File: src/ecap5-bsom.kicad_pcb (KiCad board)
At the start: 6 copper layers, 69.6 x 30 mm, 178 parts, among them J13 DDR4_SODIMM_Board, U1 TPS565242DRDR, U10 IS42S16160J-*BL, U11 IS43DR86400E, U12 ASFC4G31M-51*, U2 TPS562202DRLR, U3 TPS562202DRLR, U4 TPS562202DRLR, U5 LM3880MF*-1AA, U6 LFE5U-85F-*BG756*, U7 XLH335040.000000I, U8 W25Q128JVPIQ, U9 IS61WV25616BLL-*BLI

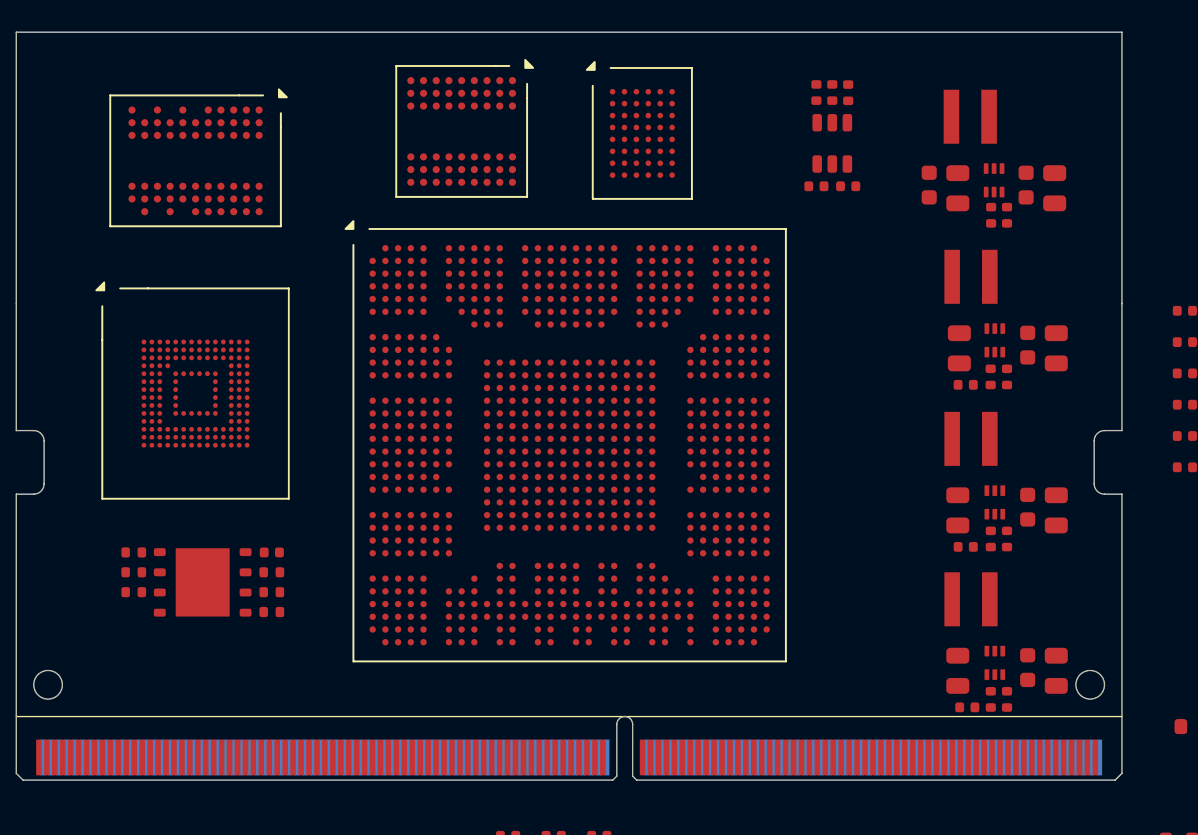
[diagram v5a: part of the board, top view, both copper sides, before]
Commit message: Starts routing power
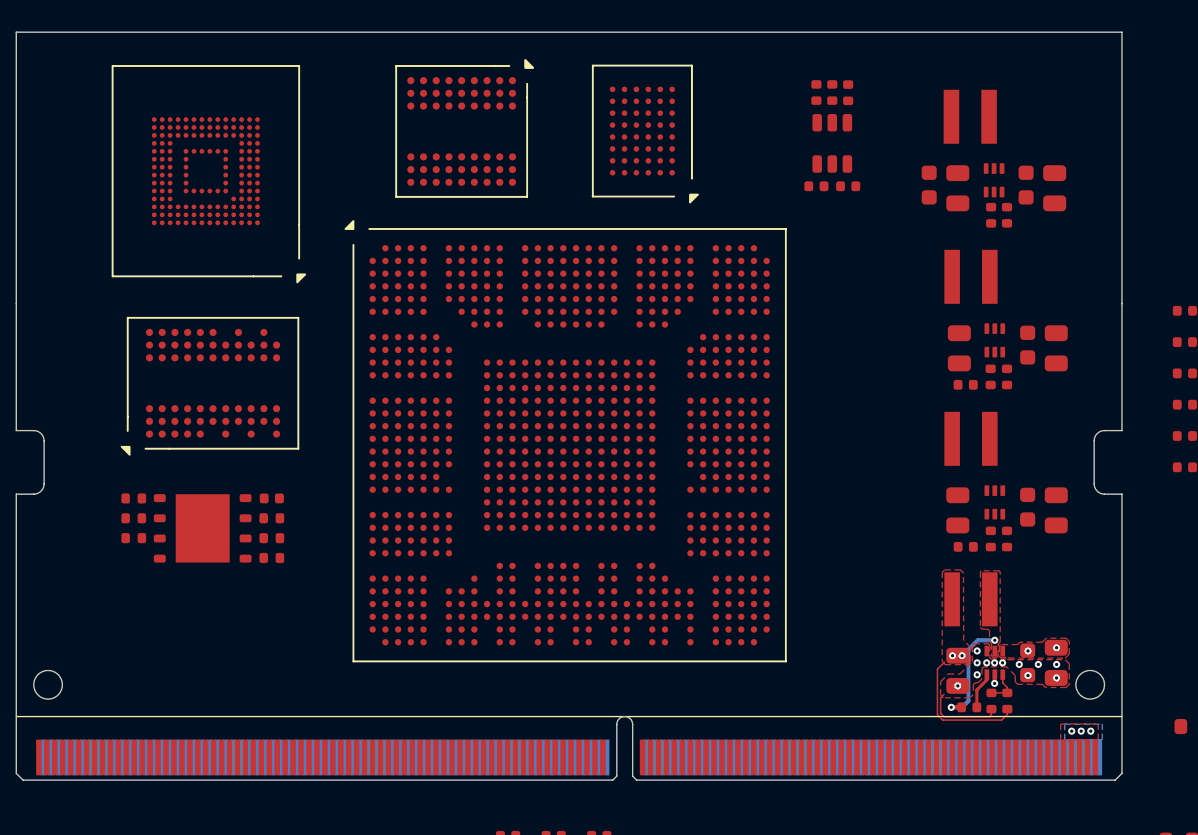
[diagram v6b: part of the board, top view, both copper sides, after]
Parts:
- moved U11 14.0 mm to (107.6, 46.1), turned to 90 degrees
- moved U12 14.0 mm to (107.2, 32.8), turned to 180 degrees
- moved C89 3.40 mm to (111.3, 53.4)
- moved R17 3.40 mm to (111.3, 57.1)
- moved R18 3.40 mm to (102.6, 54.6)
- moved R19 3.40 mm to (102.6, 55.9)
- moved R20 3.40 mm to (111.3, 54.6)
- moved R21 3.40 mm to (102.6, 53.4)
- moved R22 3.40 mm to (111.3, 55.9)
- moved U8 3.40 mm to (107.0, 55.2)
- moved R33 1.04 mm to (157.6, 66.1)
- moved R34 0.99 mm to (156.6, 66.1)
- moved C13 0.50 mm to (160.7, 63.7)
- moved C14 0.30 mm to (158.9, 63.7)
- moved U9 0.15 mm to (134.6, 30.2), turned to 180 degrees
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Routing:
- net +3V3: track 0.00 -> 8.53 mm, vias 0 -> 2
- net Net-(U4-SW): track 0.00 -> 7.04 mm, vias 0 -> 2
- net GND: track 0.00 -> 4.96 mm, vias 0 -> 12
- net Net-(U4-BST): track 0.00 -> 2.32 mm
- net Net-(U4-FB): track 0.00 -> 2.27 mm
- net VIN9_15: track 0.00 -> 0.56 mm, vias 0 -> 6
- added copper zone on F.Cu, net +3V3
- added copper zone on F.Cu, net GND
- added copper zone on F.Cu, net Net-(U4-SW)
- added copper zone on B.Cu, net VIN9_15
- added copper zone on F.Cu, net VIN9_15

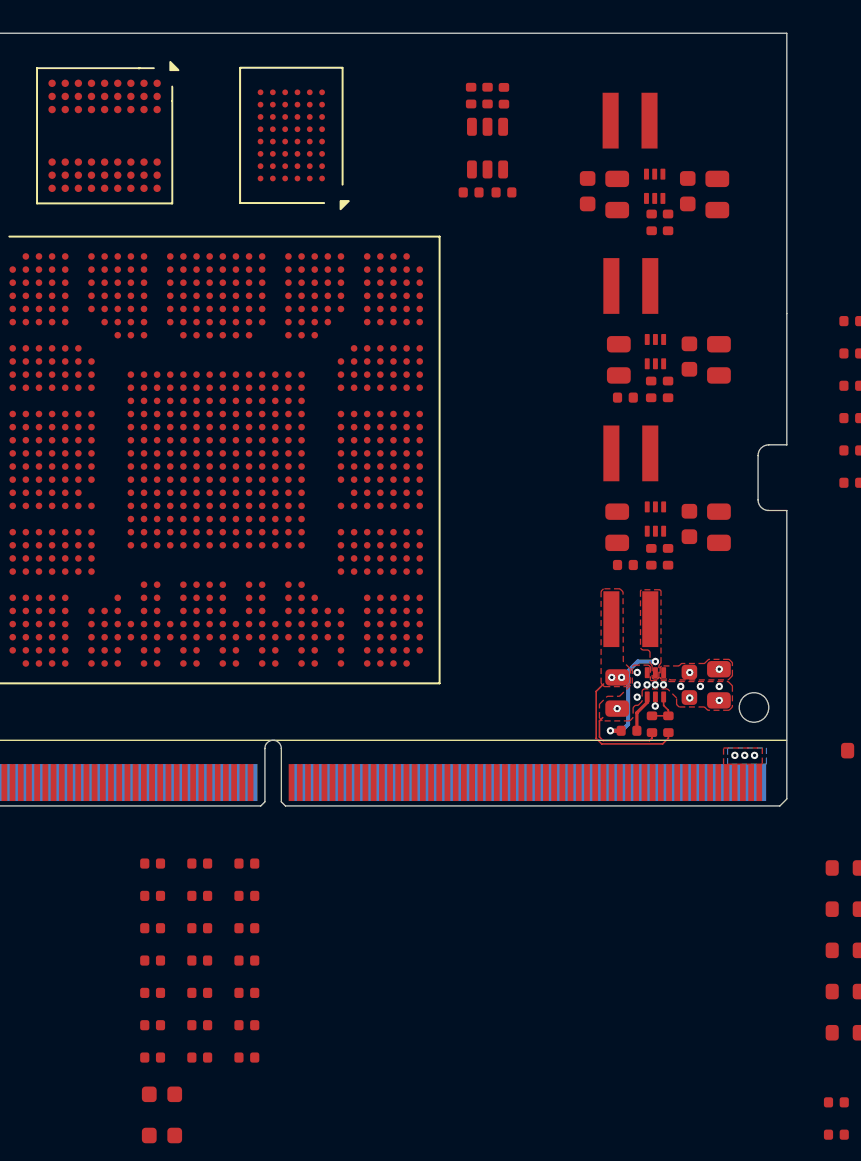
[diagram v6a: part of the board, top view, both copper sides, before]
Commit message: Start adding power planes
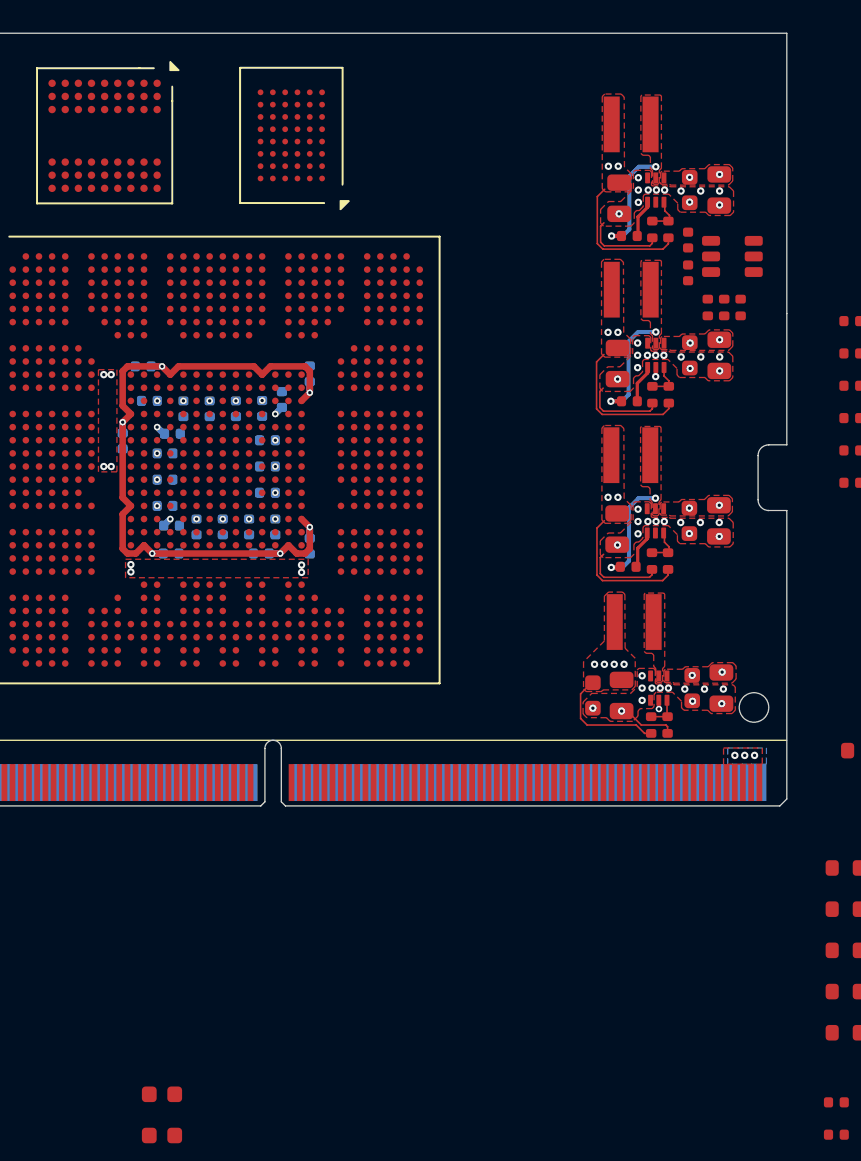
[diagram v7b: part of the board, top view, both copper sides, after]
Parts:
- added C132: 100n, Capacitor_SMD:C_0402_1005Metric, B.Cu at (125.6, 44.3)
- added C133: 100n, Capacitor_SMD:C_0402_1005Metric, B.Cu at (132.8, 55.7)
- added C134: 100n, Capacitor_SMD:C_0402_1005Metric, B.Cu at (135.8, 44.8)
- C24, C25, C26, C27, C28, C29, C30, C31, C32, C36, C37, C38, C39, C40, C41, C42, C43, C44, C45, C46, C47: moved to B.Cu
- moved C30 40.9 mm to (134.1, 46.3), turned to 90 degrees
- moved C40 39.5 mm to (129.7, 46.9), turned to -90 degrees
- moved C39 38.2 mm to (126.0, 46.4), turned to 180 degrees
- moved C47 37.1 mm to (126.9, 49.6)
- moved C27 34.0 mm to (131.2, 46.9), turned to -90 degrees
- moved C29 33.2 mm to (126.9, 51.2)
- moved C46 32.0 mm to (126.9, 52.8)
- moved C7 30.7 mm to (153.0, 64.3)
- moved R5 30.6 mm to (156.6, 66.2)
- moved R7 30.6 mm to (157.6, 66.2)
- moved U1 30.6 mm to (157.0, 63.9)
- moved L1 30.6 mm to (155.5, 59.9)
- moved C1 30.5 mm to (154.8, 64.3)
- moved C5 30.3 mm to (159.1, 63.9)
- moved C3 30.1 mm to (160.8, 63.9)
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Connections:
- C24 pad 2: Net-(C24-Pad2) -> GND
- C25 pad 2: Net-(C24-Pad2) -> GND
- C26 pad 2: Net-(C24-Pad2) -> GND
- C27 pad 2: Net-(C24-Pad2) -> GND
- C28 pad 2: Net-(C24-Pad2) -> GND
- C29 pad 2: Net-(C24-Pad2) -> GND
- C30 pad 2: Net-(C24-Pad2) -> GND
- C31 pad 2: Net-(C24-Pad2) -> GND
- C32 pad 2: Net-(C24-Pad2) -> GND
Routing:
- net +2V5: track 0.00 -> 53.1 mm, vias 0 -> 8
- net GND: track 4.96 -> 18.4 mm, vias 12 -> 49
- net +1V1: track 0.00 -> 8.95 mm, vias 0 -> 22
- net +1V8: track 0.00 -> 8.46 mm, vias 0 -> 2
- net Net-(U3-SW): track 0.00 -> 7.04 mm, vias 0 -> 2
- net Net-(U2-SW): track 0.00 -> 7.04 mm, vias 0 -> 2
- net Net-(U2-BST): track 0.00 -> 2.34 mm
- net Net-(U3-BST): track 0.00 -> 2.34 mm
- net Net-(U2-FB): track 0.00 -> 2.27 mm
- net Net-(U3-FB): track 0.00 -> 2.27 mm
- net Net-(U1-FB): track 0.00 -> 2.11 mm
- net /Power/en_1v1: track 0.00 -> 0.54 mm, vias 0 -> 1
- net +3V3: vias 2 -> 10
- net VIN9_15: vias 6 -> 12
- added copper zone on F.Cu, net +1V1
- added copper zone on In2.Cu, net +1V1
- added copper zone on F.Cu, net +1V8
- added copper zone on In2.Cu, net +1V8
- added copper zone on F.Cu, net +2V5
- added copper zone on In2.Cu, net +2V5
- added copper zone on In2.Cu, net +3V3
- added copper zone on In1.Cu, net GND
- added copper zone on In4.Cu, net GND
- added copper zone on F.Cu, net Net-(U1-SW)
- added copper zone on F.Cu, net Net-(U2-SW)
- added copper zone on F.Cu, net Net-(U3-SW)

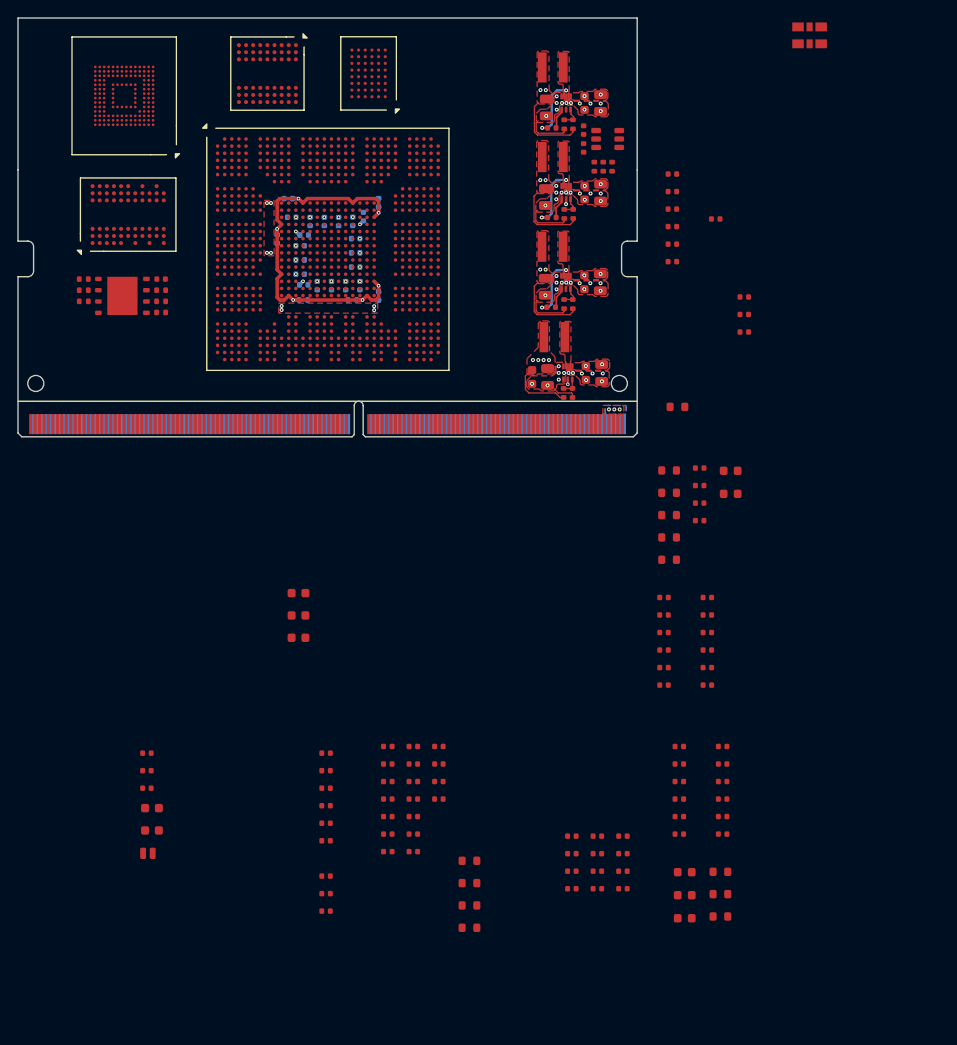
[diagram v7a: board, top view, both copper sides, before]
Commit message: Adds decoupling capacitors
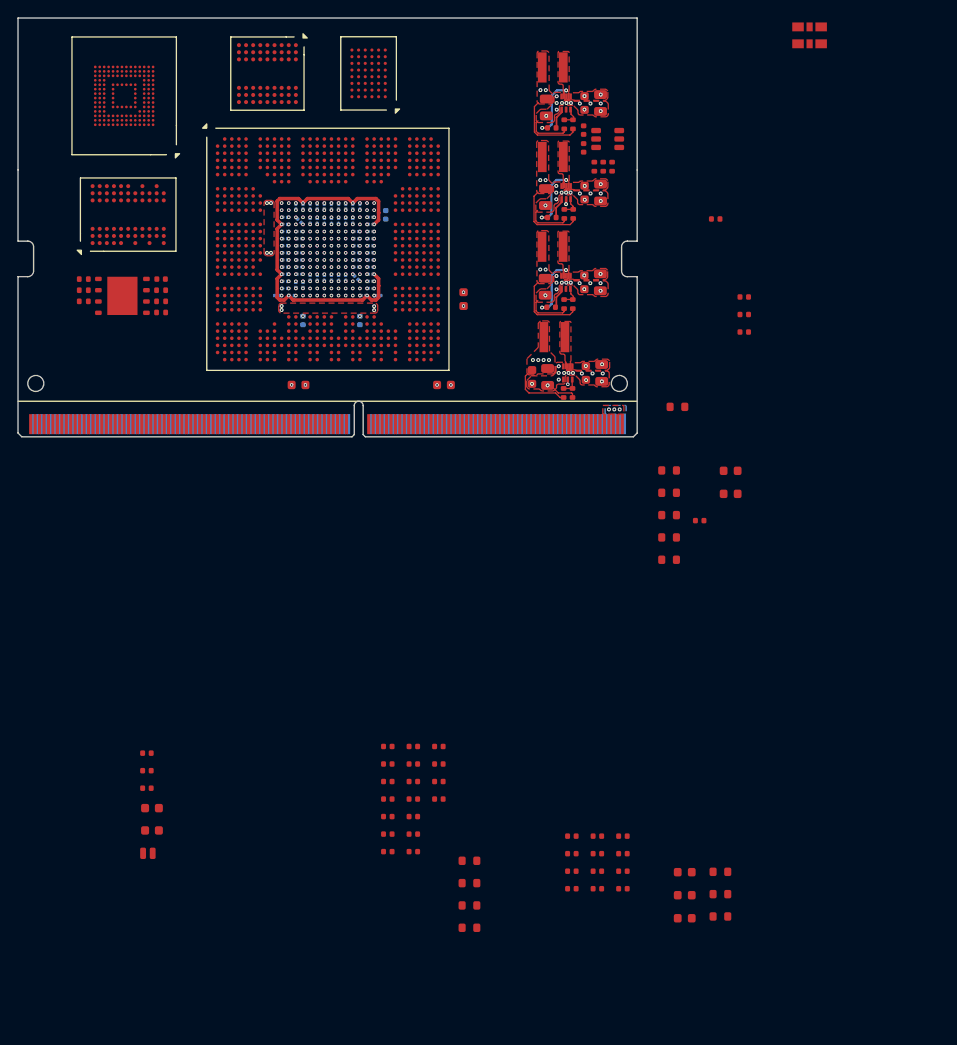
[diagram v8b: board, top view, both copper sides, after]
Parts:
- added C135: 470n, Capacitor_SMD:C_0201_0603Metric, B.Cu at (126.5, 54.0)
- added C136: 1u, Capacitor_SMD:C_0402_1005Metric, B.Cu at (133.7, 58.0)
- added C137: 1u, Capacitor_SMD:C_0402_1005Metric, B.Cu at (127.2, 58.0)
- C129, C130, C131, C50, C51, C52, C53, C56, C57, C58, C59, C62, C63, C64, C65, C68, C69, C70, C71, C74, C75, C76, C77, C80, C81, C82, C83, C84, C85: footprint Capacitor_SMD:C_0402_1005Metric -> Capacitor_SMD:C_0201_0603Metric; moved to B.Cu
- C132, C133, C134, C24, C25, C26, C27, C28, C29, C30, C31, C32, C36, C37, C39, C40, C41, C42, C43, C44, C45, C46, C47: footprint Capacitor_SMD:C_0402_1005Metric -> Capacitor_SMD:C_0201_0603Metric
- C48, C49, C54, C55, C60, C61, C66, C67, C72, C73: value 100n -> 10n; footprint Capacitor_SMD:C_0402_1005Metric -> Capacitor_SMD:C_0201_0603Metric; moved to B.Cu
- C78, C79, C86: value 100n -> 470n; footprint Capacitor_SMD:C_0402_1005Metric -> Capacitor_SMD:C_0201_0603Metric; moved to B.Cu
- moved C65 75.4 mm to (134.8, 48.8), turned to 180 degrees
- moved C71 75.0 mm to (134.8, 52.0), turned to 180 degrees
- moved C64 74.4 mm to (134.8, 48.0), turned to 180 degrees
- moved C70 74.0 mm to (134.8, 51.2), turned to 180 degrees
- moved C61 72.9 mm to (126.9, 48.8)
- moved C62 72.3 mm to (134.8, 46.4), turned to 180 degrees
- moved C68 71.4 mm to (134.8, 50.4), turned to 180 degrees
- moved C53 71.3 mm to (128.8, 45.2), turned to -90 degrees
- moved C63 71.2 mm to (134.8, 49.6), turned to 180 degrees
- moved C67 70.7 mm to (129.7, 53.2), turned to 90 degrees
- moved C131 70.4 mm to (127.2, 54.0), turned to -90 degrees
- moved C69 70.4 mm to (134.8, 53.6), turned to 180 degrees
- moved C66 69.7 mm to (133.2, 49.6), turned to 180 degrees
- moved C52 69.3 mm to (128.1, 45.2), turned to -90 degrees
- moved C130 68.2 mm to (134.8, 54.4), turned to 180 degrees
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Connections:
- C131 pad 1: +3V3 -> +1V1
- C48 pad 1: +3V3 -> +1V1
- C49 pad 1: +3V3 -> +1V1
- C54 pad 1: +3V3 -> +1V1
- C55 pad 1: +3V3 -> +1V1
- C60 pad 1: +2V5 -> +1V1
- C61 pad 1: +2V5 -> +1V1
- C66 pad 1: +2V5 -> +1V1
- C67 pad 1: +2V5 -> +1V1
- C72 pad 1: +3V3 -> +1V1
- C73 pad 1: +3V3 -> +1V1
- C78 pad 1: +1V8 -> +2V5
- C79 pad 1: +1V8 -> +2V5
- C86 pad 1: +3V3 -> +2V5
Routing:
- net +2V5: track 53.1 -> 50.7 mm, vias 8 -> 18
- net +1V1: track 8.95 -> 7.21 mm, vias 22 -> 45
- net GND: vias 49 -> 176
- net +3V3: vias 10 -> 26
- net +1V8: vias 2 -> 6
